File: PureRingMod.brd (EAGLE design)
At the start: 99 x 69.5 mm, 36 parts, among them IC1 TL074P, IC2 TL072P, X1 NC3FD-V

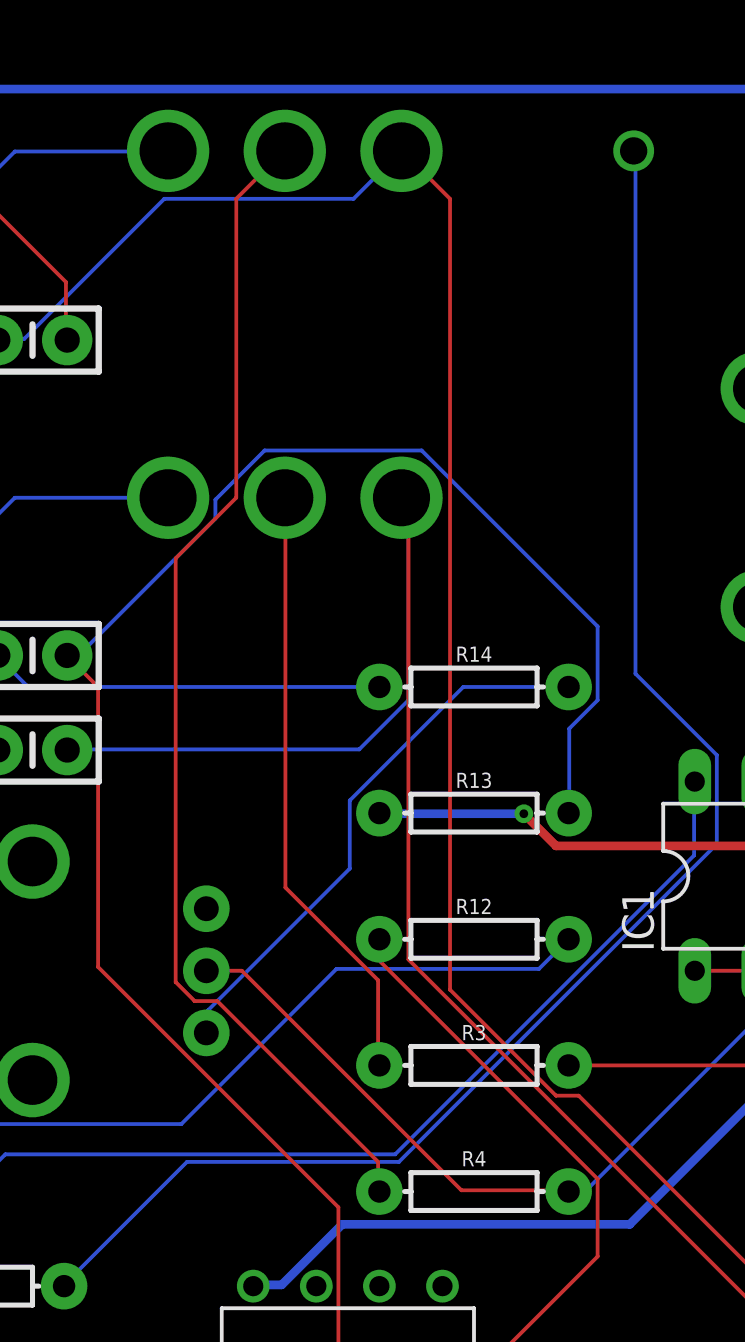
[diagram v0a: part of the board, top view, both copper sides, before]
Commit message: added mix control
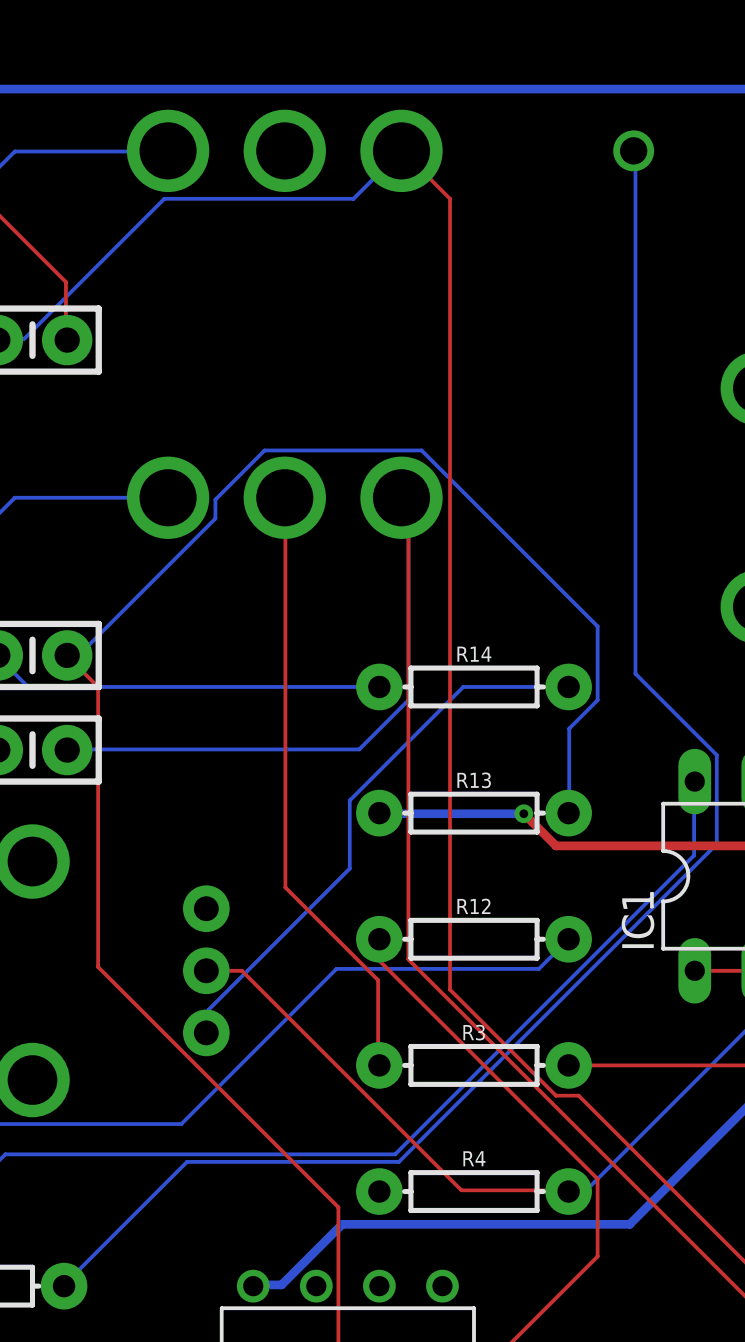
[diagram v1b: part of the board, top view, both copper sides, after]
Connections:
- net GND: now also MICVOL.P$1, R4.P$2
- net N$30: no longer R4.P$2
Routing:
- net N$8: track 47.7 -> 0.00 mm
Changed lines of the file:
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@@
 <wire x1="80.01" y1="59.7408" x2="80.16" y2="59.69" width="0.35" layer="16"/>
 <via x="64.2366" y="32.9946" extent="1-16" drill="0.35"/>
+<contactref element="MICVOL" pad="P$1"/>
+<contactref element="R4" pad="P$2"/>
+<wire x1="69.85" y1="8.89" x2="66.04" y2="17.78" width="0" layer="19" extent="1-1"/>
+<wire x1="51.45" y1="29.17" x2="58.42" y2="33.02" width="0" layer="19" extent="1-1"/>
 </signal>
 <signal name="N$9">
@@
 <wire x1="38.1" y1="14.0208" x2="38.1" y2="13.97" width="0.1524" layer="16"/>
 </signal>
-<signal name="N$13">
-<contactref element="R4" pad="P$1"/>
-<contactref element="CARRIERAC" pad="2"/>
-<wire x1="58.3692" y1="18.9738" x2="58.3692" y2="17.8308" width="0.1524" layer="1"/>
-<wire x1="51.8922" y1="25.4508" x2="58.3692" y2="18.9738" width="0.1524" layer="1"/>
-<wire x1="50.9778" y1="25.4508" x2="51.8922" y2="25.4508" width="0.1524" layer="1"/>
-<wire x1="50.2158" y1="26.2128" x2="50.9778" y2="25.4508" width="0.1524" layer="1"/>
-<wire x1="50.2158" y1="43.2816" x2="50.2158" y2="26.2128" width="0.1524" layer="1"/>
-<wire x1="52.6542" y1="45.72" x2="50.2158" y2="43.2816" width="0.1524" layer="1"/>
-<wire x1="52.6542" y1="57.7596" x2="52.6542" y2="45.72" width="0.1524" layer="1"/>
-<wire x1="54.5592" y1="59.6646" x2="52.6542" y2="57.7596" width="0.1524" layer="1"/>
-<wire x1="58.3692" y1="17.8308" x2="58.42" y2="17.78" width="0.1524" layer="1"/>
-<wire x1="54.5592" y1="59.6646" x2="54.61" y2="59.69" width="0.1524" layer="1"/>
-</signal>
 <signal name="N$14">
 <contactref element="R3" pad="P$1"/>
@@
 <contactref element="MICVOL" pad="P$2"/>
 <contactref element="IC1" pad="3"/>
-<contactref element="R4" pad="P$2"/>
 <wire x1="75.5904" y1="26.67" x2="76.2" y2="26.67" width="0.1524" layer="16"/>
 <wire x1="66.7512" y1="17.8308" x2="75.5904" y2="26.67" width="0.1524" layer="16"/>
 <wire x1="66.0654" y1="17.8308" x2="66.7512" y2="17.8308" width="0.1524" layer="16"/>
-<wire x1="66.0654" y1="17.8308" x2="66.04" y2="17.78" width="0.1524" layer="16"/>
 <wire x1="52.8828" y1="26.67" x2="51.5112" y2="26.67" width="0.1524" layer="1"/>
 <wire x1="61.722" y1="17.8308" x2="52.8828" y2="26.67" width="0.1524" layer="1"/>
 <wire x1="65.9892" y1="17.8308" x2="61.722" y2="17.8308" width="0.1524" layer="1"/>
 <wire x1="51.5112" y1="26.67" x2="51.45" y2="26.67" width="0.1524" layer="1"/>
-<wire x1="65.9892" y1="17.8308" x2="66.04" y2="17.78" width="0.1524" layer="1"/>
+<wire x1="65.9892" y1="17.8308" x2="66.0654" y2="17.8308" width="0" layer="19" extent="1-16"/>
+</signal>
+<signal name="N$8">
+<contactref element="CARRIERAC" pad="2"/>
+<contactref element="R4" pad="P$1"/>
+<wire x1="58.42" y1="17.78" x2="54.61" y2="59.69" width="0" layer="19" extent="1-1"/>
 </signal>
 </signals>

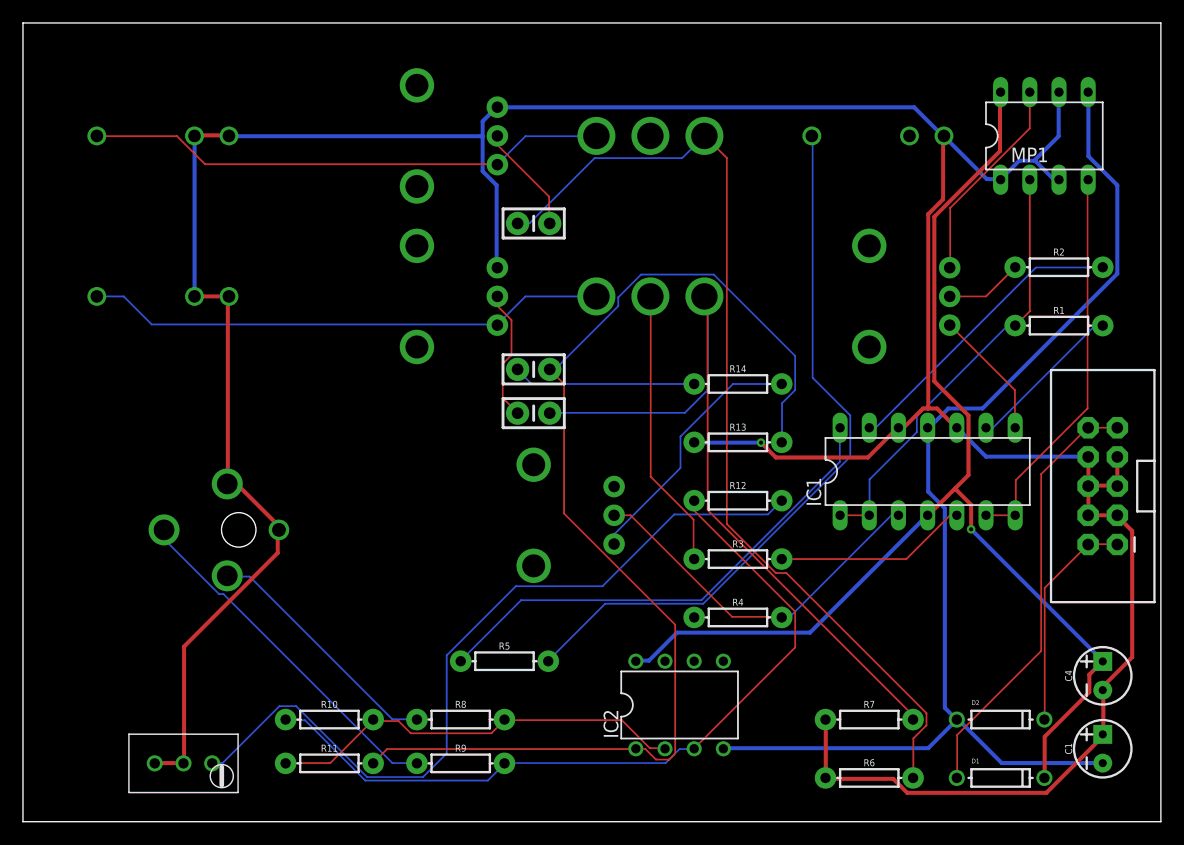
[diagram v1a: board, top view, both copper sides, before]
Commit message: updated components in feedback circuit of preamp
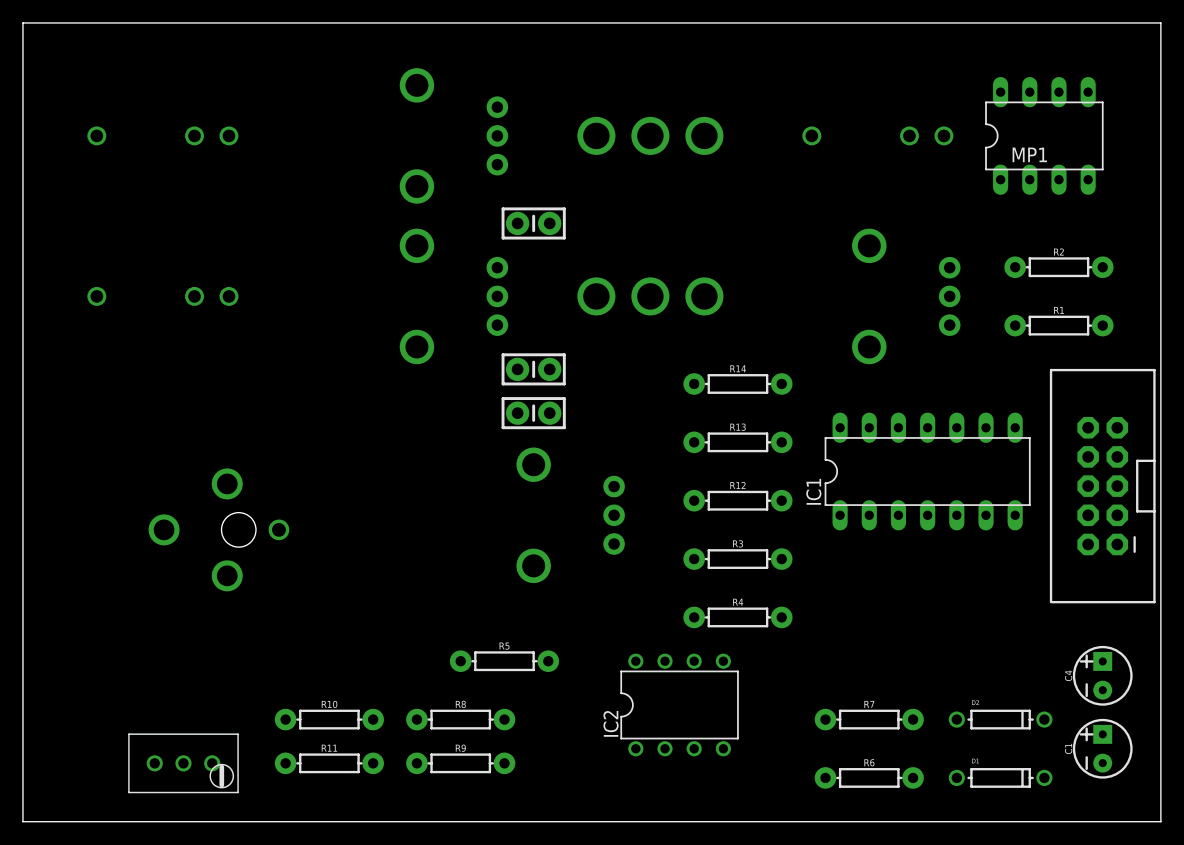
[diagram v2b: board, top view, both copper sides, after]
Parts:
- R12: value 301K -> 330K
- TR1: value 25K -> 10K
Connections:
- net GND: now also OUTPUT.NORM
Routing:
- net GND: track 294.1 -> 0.00 mm, vias 1 -> 0
- net +12V: track 105.3 -> 0.00 mm, vias 1 -> 0
- net N$27: track 101.6 -> 0.00 mm
- net -12V: track 101.0 -> 0.00 mm
- net N$20: track 84.4 -> 0.00 mm
- net N$28: track 69.1 -> 0.00 mm
- net N$25: track 67.8 -> 0.00 mm
- net N$21: track 67.3 -> 0.00 mm
- net N$15: track 63.0 -> 0.00 mm
- net N$17: track 45.6 -> 0.00 mm
- net N$16: track 45.5 -> 0.00 mm
- net N$12: track 43.2 -> 0.00 mm
- net N$1: track 38.0 -> 0.00 mm
- net N$9: track 37.8 -> 0.00 mm
- net N$24: track 36.8 -> 0.00 mm
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
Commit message: Corrected values on input circuit
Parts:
- C2, C3: value 0.1uF -> 1uF
- R6, R7: value 6k2 -> 1M
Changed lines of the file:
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@@
 <element name="VRCARIER" library="GMSN" package="POT" value="9MMPOT" x="34.29" y="59.69" rot="MR270"/>
 <element name="VRMOD" library="GMSN" package="POT" value="9MMPOT" x="34.29" y="45.72" rot="MR270"/>
-<element name="C2" library="SparkFun-Capacitors" package="CAP-PTH-SMALL-KIT" value="0.1uF" x="44.45" y="52.07" rot="R180">
+<element name="C2" library="SparkFun-Capacitors" package="CAP-PTH-SMALL-KIT" value="1uF" x="44.45" y="52.07" rot="R180">
 <attribute name="PROD_ID" value="CAP-08370" x="44.45" y="52.07" size="1.778" layer="27" rot="R180" display="off"/>
 </element>
-<element name="C3" library="SparkFun-Capacitors" package="CAP-PTH-SMALL-KIT" value="0.1uF" x="44.45" y="35.56">
+<element name="C3" library="SparkFun-Capacitors" package="CAP-PTH-SMALL-KIT" value="1uF" x="44.45" y="35.56">
 <attribute name="PROD_ID" value="CAP-08370" x="44.45" y="35.56" size="1.778" layer="27" display="off"/>
 </element>
-<element name="R6" library="SparkFun-Resistors" package="AXIAL-0.3" value="6k2" x="73.66" y="3.81">
+<element name="R6" library="SparkFun-Resistors" package="AXIAL-0.3" value="1M" x="73.66" y="3.81">
 <attribute name="PROD_ID" value="RES-8371" x="73.66" y="3.81" size="1.778" layer="27" display="off"/>
 </element>
-<element name="R7" library="SparkFun-Resistors" package="AXIAL-0.3" value="6k2" x="73.66" y="8.89">
+<element name="R7" library="SparkFun-Resistors" package="AXIAL-0.3" value="1M" x="73.66" y="8.89">
 <attribute name="PROD_ID" value="RES-8371" x="73.66" y="8.89" size="1.778" layer="27" display="off"/>
 </element>

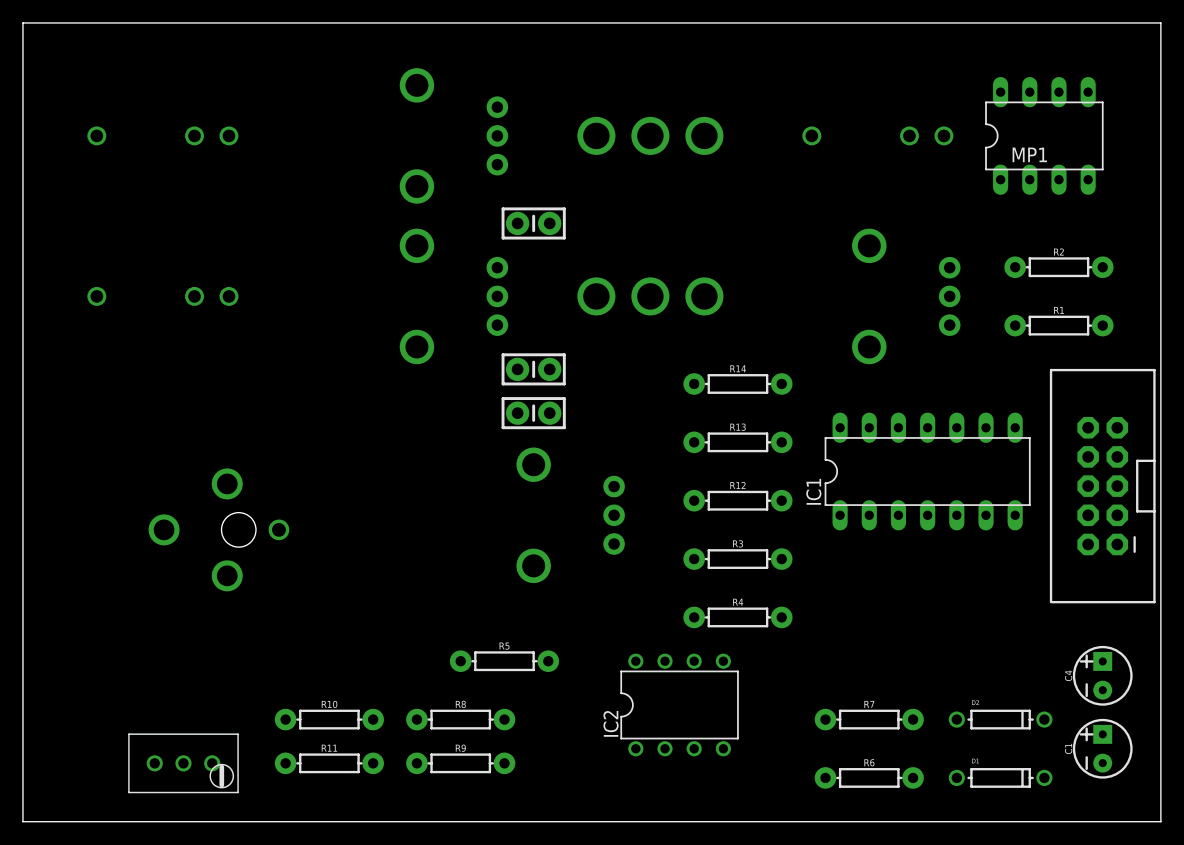
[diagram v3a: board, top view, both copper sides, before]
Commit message: corrected input components
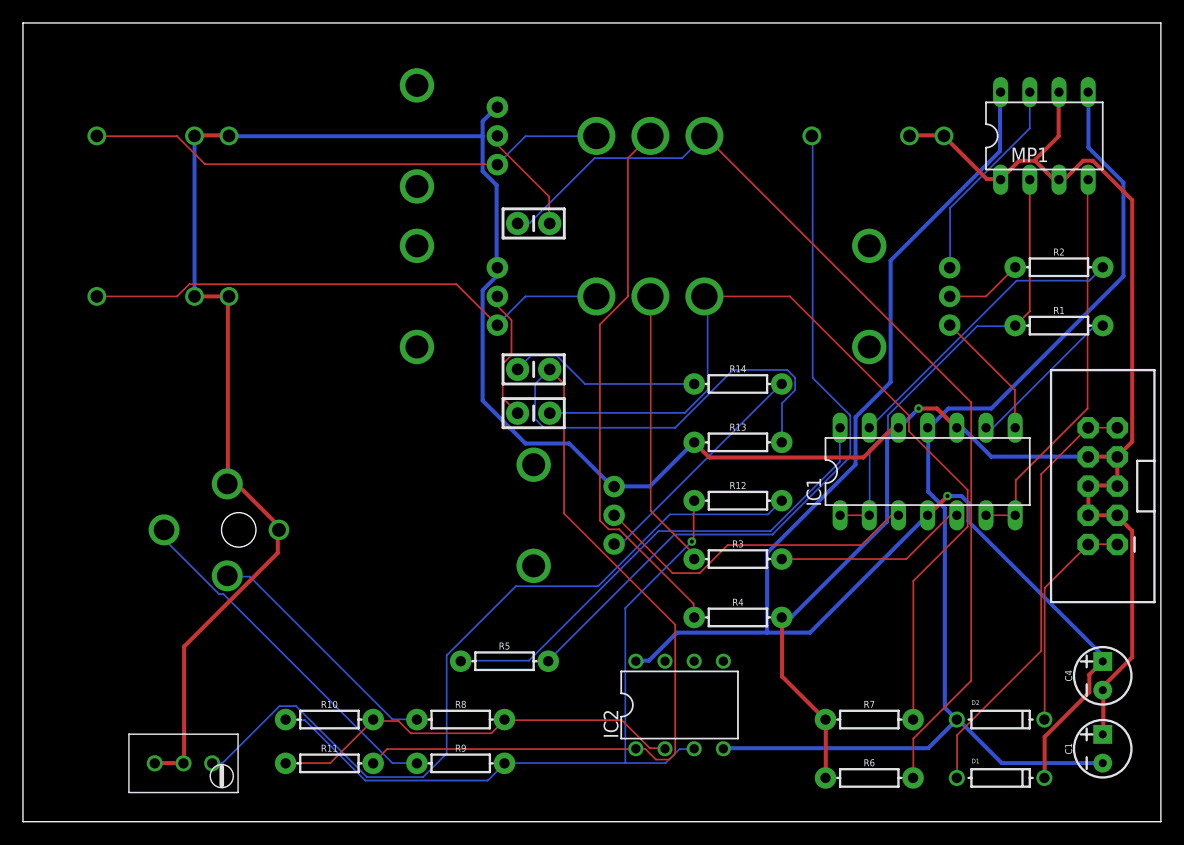
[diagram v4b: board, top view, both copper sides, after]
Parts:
- R3, R4: value 6k2 -> 4k7
- renumbered MICVOL to MICMIX, VRCARIER to VOLCARIER, VRMOD to VOLMOD
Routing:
- net GND: track 0.00 -> 304.3 mm, vias 0 -> 1
- net +12V: track 0.00 -> 121.6 mm, vias 0 -> 1
- net -12V: track 0.00 -> 101.9 mm
- net N$27: track 0.00 -> 101.6 mm
- net N$20: track 0.00 -> 87.1 mm
- net N$21: track 0.00 -> 75.5 mm
- net N$28: track 0.00 -> 69.1 mm
- net N$25: track 0.00 -> 64.3 mm, vias 0 -> 1
- net N$15: track 0.00 -> 63.0 mm
- net N$8: track 0.00 -> 47.7 mm
- net N$17: track 0.00 -> 46.5 mm
- net N$16: track 0.00 -> 45.5 mm
- net N$12: track 0.00 -> 43.2 mm
- net N$1: track 0.00 -> 39.5 mm
- net N$9: track 0.00 -> 37.8 mm
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
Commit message: added missing parts
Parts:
- added R15: 10K, SparkFun-Resistors:AXIAL-0.3
- added R16: 27K, SparkFun-Resistors:AXIAL-0.3
- R1: value 30K -> 20K
- R2: value 38K3 -> 27K
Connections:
- net N$12: now also R16.P$2
- net N$4: now also R15.P$2
- net N$5: now also R15.P$1
- net N$7: now also R16.P$1
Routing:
- net N$7: track 26.1 -> 69.9 mm, vias 0 -> 1
- net N$28: track 69.1 -> 59.0 mm, vias 0 -> 2
- net +12V: track 121.6 -> 113.8 mm, vias 1 -> 0
- net N$27: track 101.6 -> 94.2 mm
- net N$5: track 13.9 -> 21.0 mm
- net -12V: track 101.9 -> 108.0 mm
- net N$25: track 64.3 -> 70.2 mm, vias 1 -> 0
- net N$20: track 87.1 -> 91.2 mm
- net N$29: track 20.4 -> 22.9 mm
- net N$21: track 75.5 -> 73.7 mm
- net GND: track 304.3 -> 302.5 mm, vias 1 -> 0
- net N$12: track 43.2 -> 41.5 mm
- net N$4: track 11.3 -> 12.4 mm
- net N$1: track 39.5 -> 40.5 mm
- net N$26: track 16.9 -> 15.9 mm
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
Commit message: Changed output circuit values
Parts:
- R1: value 20K -> 100K
- R15: value 10K -> 20K
- R16: value 27K -> 100K
- R2: value 27K -> 20K
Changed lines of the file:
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@@
 <attribute name="NAME" x="66.04" y="48.26" size="1.27" layer="22" rot="MR270"/>
 </element>
-<element name="R1" library="SparkFun-Resistors" package="AXIAL-0.3" value="20K" x="90.17" y="43.18">
+<element name="R1" library="SparkFun-Resistors" package="AXIAL-0.3" value="100K" x="90.17" y="43.18">
 <attribute name="NAME" x="90.17" y="44.196" size="0.6096" layer="25" font="vector" ratio="20" align="bottom-center"/>
 <attribute name="PROD_ID" value="RES-8371" x="90.17" y="43.18" size="1.778" layer="27" display="off"/>
 <attribute name="VALUE" x="90.17" y="42.164" size="0.6096" layer="27" font="vector" ratio="20" align="top-center"/>
 </element>
-<element name="R2" library="SparkFun-Resistors" package="AXIAL-0.3" value="27K" x="90.17" y="48.26">
+<element name="R2" library="SparkFun-Resistors" package="AXIAL-0.3" value="20K" x="90.17" y="48.26">
 <attribute name="NAME" x="90.17" y="49.276" size="0.6096" layer="25" font="vector" ratio="20" align="bottom-center"/>
 <attribute name="PROD_ID" value="RES-8371" x="90.17" y="48.26" size="1.778" layer="27" display="off"/>
@@
 <attribute name="NAME" x="36.83" y="29.21" size="1.27" layer="22" rot="MR270"/>
 </element>
-<element name="R15" library="SparkFun-Resistors" package="AXIAL-0.3" value="10K" x="82.55" y="39.37">
+<element name="R15" library="SparkFun-Resistors" package="AXIAL-0.3" value="20K" x="82.55" y="39.37">
 <attribute name="NAME" x="82.55" y="40.386" size="0.6096" layer="25" font="vector" ratio="20" align="bottom-center"/>
 <attribute name="PROD_ID" value="RES-8371" x="82.55" y="39.37" size="1.778" layer="27" display="off"/>
 <attribute name="VALUE" x="82.55" y="38.354" size="0.6096" layer="27" font="vector" ratio="20" align="top-center"/>
 </element>
-<element name="R16" library="SparkFun-Resistors" package="AXIAL-0.3" value="27K" x="41.91" y="17.78">
+<element name="R16" library="SparkFun-Resistors" package="AXIAL-0.3" value="100K" x="41.91" y="17.78">
 <attribute name="NAME" x="41.91" y="18.796" size="0.6096" layer="25" font="vector" ratio="20" align="bottom-center"/>
 <attribute name="PROD_ID" value="RES-8371" x="41.91" y="17.78" size="1.778" layer="27" display="off"/>

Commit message: modified input mic circuit
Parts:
- removed TR1: 10K, INSTRUO:TRIMMER_TH3
- R11: value 316K -> 1M
- R12: value 330K -> 1M
- R8, R9: value 1K -> 330
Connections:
- removed net N$28: R12.P$2, TR1.1
- net GND: now also R12.P$2; no longer TR1.2, TR1.3
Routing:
- net N$28: track 59.0 -> 0.00 mm, vias 2 -> 0
- net GND: track 302.5 -> 299.8 mm
